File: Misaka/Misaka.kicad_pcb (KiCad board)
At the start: 2 copper layers, 100 x 100 mm, 106 parts, among them J1 Conn_Coaxial_Power, J2 Conn_01x04_Male, J3 Conn_01x04_Male, J4 Conn_01x04_Male, J5 USB_B_Micro, J6 Conn_01x04_Female, J7 Conn_01x04_Female_UART, J8 Conn_02x04_Odd_Even, J9 Conn_01x07, SW1 SW_DIP_x03, U1 DRV8825PWPR, U2 ATmega2560-16AU, U3 DRV8825PWPR, U4 DRV8825PWPR, U5 CH340C, U6 AMS1117-5.0, U7 AMS1117-3.3, U8 24LC02, Y1 CSTLS16M0X51-B0

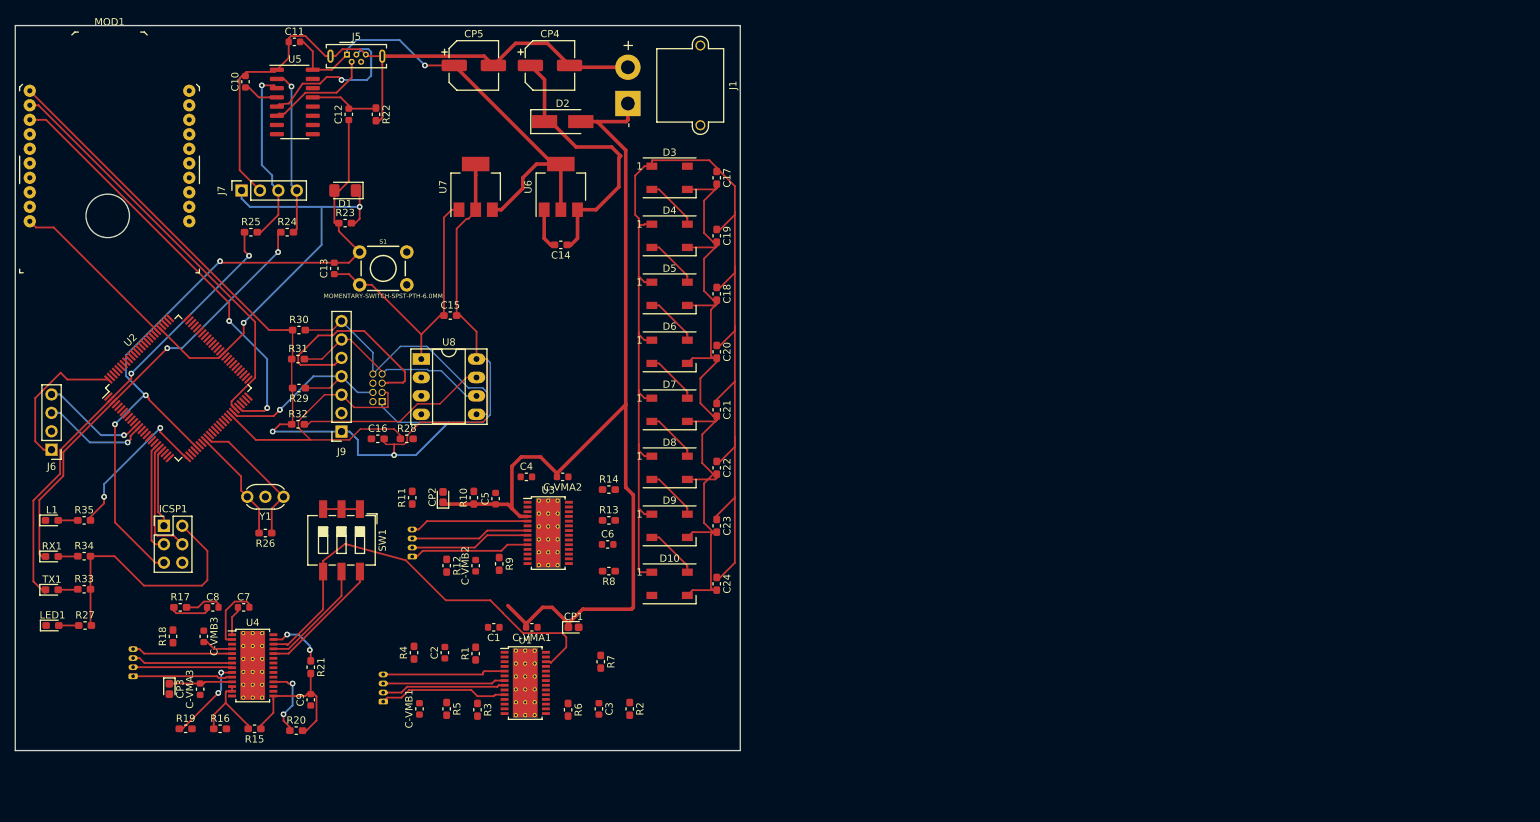
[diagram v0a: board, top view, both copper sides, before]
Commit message: change footprint to handsolding
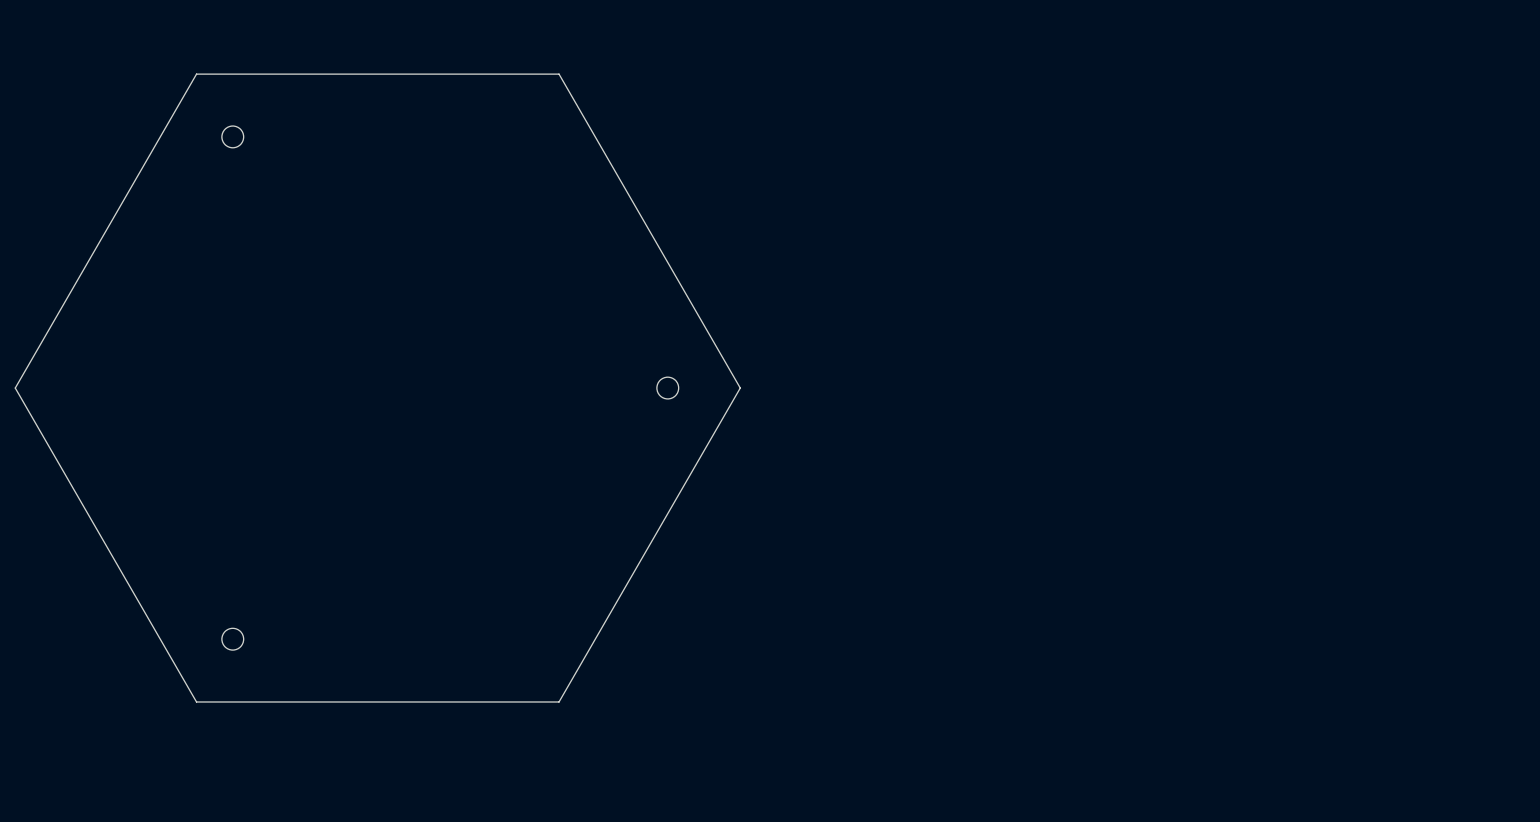
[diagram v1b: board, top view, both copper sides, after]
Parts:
- removed C-VMA1, C-VMA2, C-VMA3, C-VMB1, C-VMB2, C-VMB3, C2, C5, C8: 0.1uF, Capacitor_SMD:C_0603_1608Metric
- removed C1, C4, C7: 0.01uF, Capacitor_SMD:C_0603_1608Metric
- removed C10, C11, C12: 100nF, Capacitor_SMD:C_0603_1608Metric
- removed C13: 22pF, Capacitor_SMD:C_0603_1608Metric
- removed C14, C17, C18, C19, C20, C21, C22, C23, C24: 100nF, Capacitor_SMD:C_0603_1608Metric_Pad1.05x0.95mm_HandSolder
- removed C15, C16: 1uF, Capacitor_SMD:C_0603_1608Metric_Pad1.05x0.95mm_HandSolder
- removed C3, C6, C9: 0.47uF, Capacitor_SMD:C_0603_1608Metric
- removed CP1, CP2, CP3: 100uF, Capacitor_Tantalum_SMD:CP_EIA-1608-08_AVX-J
- removed CP4, CP5: 47uF, Capacitor_SMD:CP_Elec_6.3x5.8
- removed D1: CD1206, Diode_SMD:D_1206_3216Metric_Pad1.42x1.75mm_HandSolder
- removed D10, D3, D4, D5, D6, D7, D8, D9: WS2812B, LED_SMD:LED_WS2812B_PLCC4_5.0x5.0mm_P3.2mm
- removed D2: M7, Diode_SMD:D_SMA_Handsoldering
- removed ICSP1: Conn_02x03_Odd_Even, Connector_PinHeader_2.54mm:PinHeader_2x03_P2.54mm_Vertical
- removed J1: Conn_Coaxial_Power, Connector_AMASS:AMASS_XT30PW-M_1x02_P2.50mm_Horizontal
- removed J2, J3, J4: Conn_01x04_Male, Connector_Molex:Molex_PicoBlade_53047-0410_1x04_P1.25mm_Vertical
- removed J5: USB_B_Micro, Connector_USB:USB_Micro-B_Wuerth_614105150721_Vertical
- removed J6: Conn_01x04_Female, Connector_PinHeader_2.54mm:PinHeader_1x04_P2.54mm_Vertical
- removed J7: Conn_01x04_Female_UART, Connector_PinSocket_2.54mm:PinSocket_1x04_P2.54mm_Vertical
- removed J8: Conn_02x04_Odd_Even, Connector_PinSocket_1.27mm:PinSocket_2x04_P1.27mm_Vertical
- removed J9: Conn_01x07, Connector_PinSocket_2.54mm:PinSocket_1x07_P2.54mm_Vertical
- removed L1, RX1, TX1: LED, LED_SMD:LED_0603_1608Metric_Pad1.05x0.95mm_HandSolder
- removed LED1: ON, LED_SMD:LED_0603_1608Metric_Pad1.05x0.95mm_HandSolder
- removed MOD1: XB24CZ7PIT-004, digikey-footprints:XBEE_PRO-20_THT
- removed R1, R10, R17, R26: 1M, Resistor_SMD:R_0603_1608Metric_Pad1.05x0.95mm_HandSolder
- removed R11, R12, R18, R19, R4, R5: 200m, Resistor_SMD:R_0603_1608Metric_Pad1.05x0.95mm_HandSolder
- removed R13, R14, R20, R21, R6, R7: 10K, Resistor_SMD:R_0603_1608Metric_Pad1.05x0.95mm_HandSolder
- removed R15, R2, R8: 50K, Resistor_SMD:R_0603_1608Metric_Pad1.05x0.95mm_HandSolder
- removed R16, R3, R9: 30K, Resistor_SMD:R_0603_1608Metric_Pad1.05x0.95mm_HandSolder
- removed R22, R24, R25, R27, R28, R33, R34, R35: 1k, Resistor_SMD:R_0603_1608Metric_Pad1.05x0.95mm_HandSolder
- removed R23: 10k, Resistor_SMD:R_0603_1608Metric_Pad1.05x0.95mm_HandSolder
- removed R29, R30, R31, R32: 4.7k, Resistor_SMD:R_0603_1608Metric_Pad1.05x0.95mm_HandSolder
- removed S1: MOMENTARY-SWITCH-SPST-PTH-6.0MM, Switches:TACTILE_SWITCH_PTH_6.0MM
- removed SW1: SW_DIP_x03, Button_Switch_SMD:SW_DIP_SPSTx03_Slide_6.7x9.18mm_W8.61mm_P2.54mm_LowProfile
- removed U1, U3, U4: DRV8825PWPR, Package_SO:HTSSOP-28-1EP_4.4x9.7mm_P0.65mm_EP3.4x9.5mm_ThermalVias
- removed U2: ATmega2560-16AU, Package_QFP:TQFP-100_14x14mm_P0.5mm
- removed U5: CH340C, Package_SO:SOIC-16_3.9x9.9mm_P1.27mm
- removed U6: AMS1117-5.0, Package_TO_SOT_SMD:SOT-223-3_TabPin2
- removed U7: AMS1117-3.3, Package_TO_SOT_SMD:SOT-223-3_TabPin2
- removed U8: 24LC02, Package_DIP:DIP-8_W7.62mm_Socket_LongPads
- removed Y1: CSTLS16M0X51-B0, Crystal:Resonator_muRata_CSTLSxxxX-3Pin_W5.5mm_H3.0mm
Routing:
- net +5V: track 357.3 -> 0.00 mm, vias 3 -> 0
- net GND: track 258.7 -> 0.00 mm
- net +3V3: track 179.3 -> 0.00 mm, vias 2 -> 0
- net +12V: track 158.8 -> 0.00 mm
- net /RESET: track 104.9 -> 0.00 mm, vias 3 -> 0
- net /RX0: track 63.5 -> 0.00 mm, vias 2 -> 0
- net /TX0: track 60.4 -> 0.00 mm, vias 2 -> 0
- net /MS3: track 59.8 -> 0.00 mm
- net /TX1: track 59.0 -> 0.00 mm, vias 2 -> 0
- net /RX1: track 57.1 -> 0.00 mm
- net /SCL: track 47.0 -> 0.00 mm
- net /CameraModule/E2PROM-SDA: track 39.1 -> 0.00 mm
- net Net-(C14-Pad1): track 38.1 -> 0.00 mm
- net /CameraModule/EFUSE: track 30.5 -> 0.00 mm
- net /CameraModule/E2PROM-SCK: track 28.8 -> 0.00 mm
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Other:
- board size 100 x 100 mm -> 100 x 86.6 mm

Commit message: route v2.0
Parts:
- added C-VMA1: 0.1uF, Capacitor_SMD:C_0603_1608Metric_Pad1.05x0.95mm_HandSolder, B.Cu at (164.3, 119.7)
- added C-VMA2: 0.1uF, Capacitor_SMD:C_0603_1608Metric_Pad1.05x0.95mm_HandSolder, B.Cu at (205.9, 121.4)
- added C-VMA3: 0.1uF, Capacitor_SMD:C_0603_1608Metric_Pad1.05x0.95mm_HandSolder, B.Cu at (229.9, 124.9)
- added C-VMB1: 0.1uF, Capacitor_SMD:C_0603_1608Metric_Pad1.05x0.95mm_HandSolder, B.Cu at (168.7, 119.7)
- added C-VMB2: 0.1uF, Capacitor_SMD:C_0603_1608Metric_Pad1.05x0.95mm_HandSolder, B.Cu at (205.7, 126.5)
- added C-VMB3: 0.1uF, Capacitor_SMD:C_0603_1608Metric_Pad1.05x0.95mm_HandSolder, B.Cu at (230.2, 122.4)
- added C1: 0.01uF, Capacitor_SMD:C_0603_1608Metric_Pad1.05x0.95mm_HandSolder, B.Cu at (181.5, 123.5)
- added C10: 100nF, Capacitor_SMD:C_0603_1608Metric_Pad1.05x0.95mm_HandSolder, F.Cu at (97.9, 101.9)
- added C11: 100nF, Capacitor_SMD:C_0603_1608Metric_Pad1.05x0.95mm_HandSolder, F.Cu at (105.6, 97.0)
- added C12: 100nF, Capacitor_SMD:C_0603_1608Metric_Pad1.05x0.95mm_HandSolder, F.Cu at (106.6, 99.5)
- added C13: 22pF, Capacitor_SMD:C_0603_1608Metric_Pad1.05x0.95mm_HandSolder, F.Cu at (102.2, 101.9)
- added C14: 100nF, Capacitor_SMD:C_0603_1608Metric_Pad1.05x0.95mm_HandSolder, F.Cu at (191.9, 86.9)
- added C15: 1uF, Capacitor_SMD:C_0603_1608Metric_Pad1.05x0.95mm_HandSolder, F.Cu at (84.7, 80.1)
- added C16: 1uF, Capacitor_SMD:C_0603_1608Metric_Pad1.05x0.95mm_HandSolder, F.Cu at (71.2, 95.4)
- added C17: 100nF, Capacitor_SMD:C_0603_1608Metric_Pad1.05x0.95mm_HandSolder, F.Cu at (202.3, 52.3)
- added C18: 100nF, Capacitor_SMD:C_0603_1608Metric_Pad1.05x0.95mm_HandSolder, F.Cu at (215.3, 52.3)
- added C19: 100nF, Capacitor_SMD:C_0603_1608Metric_Pad1.05x0.95mm_HandSolder, F.Cu at (211.0, 52.3)
- added C2: 0.1uF, Capacitor_SMD:C_0603_1608Metric_Pad1.05x0.95mm_HandSolder, B.Cu at (181.5, 131.0)
- added C20: 100nF, Capacitor_SMD:C_0603_1608Metric_Pad1.05x0.95mm_HandSolder, F.Cu at (215.3, 49.8)
- added C21: 100nF, Capacitor_SMD:C_0603_1608Metric_Pad1.05x0.95mm_HandSolder, F.Cu at (206.7, 49.8)
- added C22: 100nF, Capacitor_SMD:C_0603_1608Metric_Pad1.05x0.95mm_HandSolder, F.Cu at (202.3, 49.8)
- added C23: 100nF, Capacitor_SMD:C_0603_1608Metric_Pad1.05x0.95mm_HandSolder, F.Cu at (206.7, 52.3)
- added C24: 100nF, Capacitor_SMD:C_0603_1608Metric_Pad1.05x0.95mm_HandSolder, F.Cu at (211.0, 49.8)
- added C3: 0.47uF, Capacitor_SMD:C_0603_1608Metric_Pad1.05x0.95mm_HandSolder, B.Cu at (181.8, 121.0)
- added C4: 0.01uF, Capacitor_SMD:C_0603_1608Metric_Pad1.05x0.95mm_HandSolder, B.Cu at (205.7, 123.9)
- added C5: 0.1uF, Capacitor_SMD:C_0603_1608Metric_Pad1.05x0.95mm_HandSolder, B.Cu at (201.6, 121.2)
- added C6: 0.47uF, Capacitor_SMD:C_0603_1608Metric_Pad1.05x0.95mm_HandSolder, B.Cu at (197.2, 121.0)
- added C7: 0.01uF, Capacitor_SMD:C_0603_1608Metric_Pad1.05x0.95mm_HandSolder, B.Cu at (221.1, 124.5)
- added C8: 0.1uF, Capacitor_SMD:C_0603_1608Metric_Pad1.05x0.95mm_HandSolder, B.Cu at (212.8, 121.1)
- added C9: 0.47uF, Capacitor_SMD:C_0603_1608Metric_Pad1.05x0.95mm_HandSolder, B.Cu at (217.1, 121.1)
- added CP1: 100uF, Capacitor_Tantalum_SMD:CP_EIA-1608-08_AVX-J_Pad1.25x1.05mm_HandSolder, B.Cu at (172.8, 125.7)
- added CP2: 100uF, Capacitor_Tantalum_SMD:CP_EIA-1608-08_AVX-J_Pad1.25x1.05mm_HandSolder, B.Cu at (196.9, 126.1)
- added CP3: 100uF, Capacitor_Tantalum_SMD:CP_EIA-1608-08_AVX-J_Pad1.25x1.05mm_HandSolder, B.Cu at (221.2, 127.1)
- added CP4: 47uF, Capacitor_SMD:CP_Elec_6.3x5.8, F.Cu at (180.1, 85.1)
- added CP5: 47uF, Capacitor_SMD:CP_Elec_6.3x5.8, F.Cu at (180.1, 76.9)
- added D1: CD1206, Diode_SMD:D_1206_3216Metric_Pad1.42x1.75mm_HandSolder, F.Cu at (84.0, 102.2)
- added D10: WS2812B, LED_SMD:LED_WS2812B_PLCC4_5.0x5.0mm_P3.2mm, F.Cu at (204.3, 45.2)
- added D2: M7, Diode_SMD:D_SMA_Handsoldering, F.Cu at (190.3, 75.1)
- added D3: WS2812B, LED_SMD:LED_WS2812B_PLCC4_5.0x5.0mm_P3.2mm, F.Cu at (229.6, 45.2)
- added D4: WS2812B, LED_SMD:LED_WS2812B_PLCC4_5.0x5.0mm_P3.2mm, F.Cu at (229.6, 38.6)
- added D5: WS2812B, LED_SMD:LED_WS2812B_PLCC4_5.0x5.0mm_P3.2mm, F.Cu at (221.2, 45.2)
- added D6: WS2812B, LED_SMD:LED_WS2812B_PLCC4_5.0x5.0mm_P3.2mm, F.Cu at (221.2, 38.6)
- added D7: WS2812B, LED_SMD:LED_WS2812B_PLCC4_5.0x5.0mm_P3.2mm, F.Cu at (204.3, 38.6)
- added D8: WS2812B, LED_SMD:LED_WS2812B_PLCC4_5.0x5.0mm_P3.2mm, F.Cu at (212.8, 45.2)
- added D9: WS2812B, LED_SMD:LED_WS2812B_PLCC4_5.0x5.0mm_P3.2mm, F.Cu at (212.8, 38.6)
- added ICSP1: Conn_02x03_Odd_Even, Connector_PinHeader_2.54mm:PinHeader_2x03_P2.54mm_Vertical, F.Cu at (182.4, 54.5)
- added J1: Conn_Coaxial_Power, Connector_AMASS:AMASS_XT30PW-M_1x02_P2.50mm_Horizontal, F.Cu at (54.8, 104.2)
- added J2: Conn_01x04_Male, Connector_Molex:Molex_PicoBlade_53047-0410_1x04_P1.25mm_Vertical, B.Cu at (173.1, 129.2)
- added J3: Conn_01x04_Male, Connector_Molex:Molex_PicoBlade_53047-0410_1x04_P1.25mm_Vertical, B.Cu at (197.2, 129.7)
- added J4: Conn_01x04_Male, Connector_Molex:Molex_PicoBlade_53047-0410_1x04_P1.25mm_Vertical, B.Cu at (221.5, 130.6)
- added J5: USB_B_Micro, Connector_USB:USB_Micro-B_Wuerth_614105150721_Vertical, F.Cu at (97.8, 90.5)
- added J6: Conn_01x04_Female, Connector_PinHeader_2.54mm:PinHeader_1x04_P2.54mm_Vertical, F.Cu at (212.9, 76.6)
- added J7: Conn_01x04_Female_UART, Connector_PinSocket_2.54mm:PinSocket_1x04_P2.54mm_Vertical, F.Cu at (83.3, 90.6)
- added J8: Conn_02x04_Odd_Even, Connector_PinSocket_1.27mm:PinSocket_2x04_P1.27mm_Vertical, B.Cu at (75.7, 76.9)
- added J9: Conn_01x07, Connector_PinSocket_2.54mm:PinSocket_1x07_P2.54mm_Vertical, F.Cu at (67.5, 71.5)
- added L1: LED, LED_SMD:LED_0603_1608Metric_Pad1.05x0.95mm_HandSolder, F.Cu at (61.3, 55.6)
- added LED1: ON, LED_SMD:LED_0603_1608Metric_Pad1.05x0.95mm_HandSolder, F.Cu at (187.5, 87.0)
- added MOD1: XB24CZ7PIT-004, digikey-footprints:XBEE_PRO-20_THT, F.Cu at (87.5, 49.5)
- added R1: 1M, Resistor_SMD:R_0603_1608Metric_Pad1.05x0.95mm_HandSolder, B.Cu at (172.7, 123.1)
- added R10: 1M, Resistor_SMD:R_0603_1608Metric_Pad1.05x0.95mm_HandSolder, B.Cu at (192.9, 120.1)
- added R11: 200m, Resistor_SMD:R_0603_1608Metric_Pad1.05x0.95mm_HandSolder, B.Cu at (196.9, 123.5)
- added R12: 200m, Resistor_SMD:R_0603_1608Metric_Pad1.05x0.95mm_HandSolder, B.Cu at (201.3, 126.2)
- added R13: 10K, Resistor_SMD:R_0603_1608Metric_Pad1.05x0.95mm_HandSolder, B.Cu at (205.7, 129.0)
- added R14: 10K, Resistor_SMD:R_0603_1608Metric_Pad1.05x0.95mm_HandSolder, B.Cu at (201.3, 123.7)
- added R15: 50K, Resistor_SMD:R_0603_1608Metric_Pad1.05x0.95mm_HandSolder, B.Cu at (225.6, 127.2)
- added R16: 30K, Resistor_SMD:R_0603_1608Metric_Pad1.05x0.95mm_HandSolder, B.Cu at (229.9, 129.9)
- added R17: 1M, Resistor_SMD:R_0603_1608Metric_Pad1.05x0.95mm_HandSolder, B.Cu at (225.6, 124.7)
- added R18: 200m, Resistor_SMD:R_0603_1608Metric_Pad1.05x0.95mm_HandSolder, B.Cu at (221.5, 122.0)
- added R19: 200m, Resistor_SMD:R_0603_1608Metric_Pad1.05x0.95mm_HandSolder, B.Cu at (229.9, 127.4)
- added R2: 50K, Resistor_SMD:R_0603_1608Metric_Pad1.05x0.95mm_HandSolder, B.Cu at (177.2, 125.8)
- added R20: 10K, Resistor_SMD:R_0603_1608Metric_Pad1.05x0.95mm_HandSolder, B.Cu at (225.8, 122.1)
- added R21: 10K, Resistor_SMD:R_0603_1608Metric_Pad1.05x0.95mm_HandSolder, B.Cu at (229.9, 132.4)
- added R22: 1k, Resistor_SMD:R_0603_1608Metric_Pad1.05x0.95mm_HandSolder, F.Cu at (105.6, 94.5)
- added R23: 10k, Resistor_SMD:R_0603_1608Metric_Pad1.05x0.95mm_HandSolder, F.Cu at (93.5, 101.9)
- added R24: 1k, Resistor_SMD:R_0603_1608Metric_Pad1.05x0.95mm_HandSolder, F.Cu at (89.2, 101.0)
- added R25: 1k, Resistor_SMD:R_0603_1608Metric_Pad1.05x0.95mm_HandSolder, F.Cu at (106.3, 89.5)
- added R26: 1M, Resistor_SMD:R_0603_1608Metric_Pad1.05x0.95mm_HandSolder, F.Cu at (47.2, 93.7)
- added R27: 1k, Resistor_SMD:R_0603_1608Metric_Pad1.05x0.95mm_HandSolder, F.Cu at (197.3, 82.4)
- added R28: 1k, Resistor_SMD:R_0603_1608Metric_Pad1.05x0.95mm_HandSolder, F.Cu at (71.2, 97.9)
- added R29: 4.7k, Resistor_SMD:R_0603_1608Metric_Pad1.05x0.95mm_HandSolder, F.Cu at (84.5, 76.5)
- added R3: 30K, Resistor_SMD:R_0603_1608Metric_Pad1.05x0.95mm_HandSolder, B.Cu at (181.5, 128.5)
- added R30: 4.7k, Resistor_SMD:R_0603_1608Metric_Pad1.05x0.95mm_HandSolder, F.Cu at (75.6, 95.4)
- added R31: 4.7k, Resistor_SMD:R_0603_1608Metric_Pad1.05x0.95mm_HandSolder, F.Cu at (71.2, 100.4)
- added R32: 4.7k, Resistor_SMD:R_0603_1608Metric_Pad1.05x0.95mm_HandSolder, F.Cu at (84.2, 72.2)
- added R33: 1k, Resistor_SMD:R_0603_1608Metric_Pad1.05x0.95mm_HandSolder, F.Cu at (65.6, 58.2)
- added R34: 1k, Resistor_SMD:R_0603_1608Metric_Pad1.05x0.95mm_HandSolder, F.Cu at (65.6, 55.6)
- added R35: 1k, Resistor_SMD:R_0603_1608Metric_Pad1.05x0.95mm_HandSolder, F.Cu at (61.2, 58.2)
- added R4: 200m, Resistor_SMD:R_0603_1608Metric_Pad1.05x0.95mm_HandSolder, B.Cu at (177.2, 123.3)
- added R5: 200m, Resistor_SMD:R_0603_1608Metric_Pad1.05x0.95mm_HandSolder, B.Cu at (173.1, 120.6)
- added R6: 10K, Resistor_SMD:R_0603_1608Metric_Pad1.05x0.95mm_HandSolder, B.Cu at (181.5, 126.0)
- added R7: 10K, Resistor_SMD:R_0603_1608Metric_Pad1.05x0.95mm_HandSolder, B.Cu at (177.4, 120.8)
- added R8: 50K, Resistor_SMD:R_0603_1608Metric_Pad1.05x0.95mm_HandSolder, B.Cu at (188.5, 120.1)
- added R9: 30K, Resistor_SMD:R_0603_1608Metric_Pad1.05x0.95mm_HandSolder, B.Cu at (205.7, 131.5)
- added RX1: LED, LED_SMD:LED_0603_1608Metric_Pad1.05x0.95mm_HandSolder, F.Cu at (56.9, 55.6)
- added S1: MOMENTARY-SWITCH-SPST-PTH-6.0MM, Switches:TACTILE_SWITCH_PTH_6.0MM, F.Cu at (98.7, 96.9)
- added SW1: SW_DIP_x03, Button_Switch_SMD:SW_DIP_SPSTx03_Slide_6.7x9.18mm_W8.61mm_P2.54mm_LowProfile, F.Cu at (203.0, 63.5)
- added TX1: LED, LED_SMD:LED_0603_1608Metric_Pad1.05x0.95mm_HandSolder, F.Cu at (56.9, 58.2)
- added U1: DRV8825PWPR, Package_SO:HTSSOP-28-1EP_4.4x9.7mm_P0.65mm_EP3.4x9.5mm_ThermalVias, B.Cu at (166.3, 126.6)
- added U2: ATmega2560-16AU, Package_QFP:TQFP-100_14x14mm_P0.5mm, F.Cu at (49.9, 76.8)
- added U3: DRV8825PWPR, Package_SO:HTSSOP-28-1EP_4.4x9.7mm_P0.65mm_EP3.4x9.5mm_ThermalVias, B.Cu at (190.5, 127.0)
- added U4: DRV8825PWPR, Package_SO:HTSSOP-28-1EP_4.4x9.7mm_P0.65mm_EP3.4x9.5mm_ThermalVias, B.Cu at (214.8, 128.0)
- added U5: CH340C, Package_SO:SOIC-16_3.9x9.9mm_P1.27mm, F.Cu at (89.8, 94.0)
- added U6: AMS1117-5.0, Package_TO_SOT_SMD:SOT-223-3_TabPin2, F.Cu at (200.3, 77.0)
- added U7: AMS1117-3.3, Package_TO_SOT_SMD:SOT-223-3_TabPin2, F.Cu at (190.2, 81.5)
- added U8: 24LC02, Package_DIP:DIP-8_W7.62mm_Socket_LongPads, F.Cu at (71.2, 84.4)
- added Y1: CSTLS16M0X51-B0, Crystal:Resonator_muRata_CSTLSxxxX-3Pin_W5.5mm_H3.0mm, F.Cu at (50.1, 89.4)
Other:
- net class Default: trace_width 0.25 -> 0.254
- net class Power added: clearance 0.254, trace_width 0.5, via_dia 1.2, via_drill 0.7
- rule trace_min: 0.2 -> 0.12

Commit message: route v2.1
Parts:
- moved ICSP1 152.1 mm to (32.1, 77.6), turned to 180 degrees
- moved C14 67.5 mm to (137.2, 47.3)
- moved CP5 67.5 mm to (125.4, 37.3)
- moved D2 67.5 mm to (135.7, 35.5)
- moved J6 67.5 mm to (158.3, 37.0)
- moved R27 67.5 mm to (142.7, 42.8)
- moved U6 67.5 mm to (145.6, 37.4)
- moved U7 67.5 mm to (135.6, 41.9)
- moved CP4 67.5 mm to (125.4, 45.5)
- moved LED1 67.5 mm to (132.9, 47.4)
- moved R35 13.4 mm to (49.0, 63.7)
- moved TX1 13.4 mm to (44.7, 63.8)
- moved L1 13.4 mm to (49.1, 61.2)
- moved R34 13.4 mm to (53.4, 61.1)
- moved RX1 13.4 mm to (44.7, 61.2)
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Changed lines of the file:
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@@
   )
   (module Package_TO_SOT_SMD:SOT-223-3_TabPin2 (layer F.Cu)
-    (at 190.22 81.53)
+    (at 135.57 41.93)
     (descr "module CMS SOT223 4 pins")
     (tags "CMS SOT")
@@
   )
   (module Package_TO_SOT_SMD:SOT-223-3_TabPin2 (layer F.Cu)
-    (at 200.27 76.98)
+    (at 145.62 37.38)
     (descr "module CMS SOT223 4 pins")
     (tags "CMS SOT")
@@
   )
   (module LED_SMD:LED_0603_1608Metric_Pad1.05x0.95mm_HandSolder (layer F.Cu)
-    (at 56.905 58.23)
+    (at 44.705 63.78)
     (descr "LED SMD 0603 (1608 Metric), square (rectangular) end terminal, IPC_7351 nominal, (Body size source: http://www.tortai-tech.com/upload/download/2011102023233369053.pdf), generated with kicad-footprint-generator")
     (tags "LED handsolder")
@@
   )
   (module LED_SMD:LED_0603_1608Metric_Pad1.05x0.95mm_HandSolder (layer F.Cu)
-    (at 56.905 55.64)
+    (at 44.705 61.19)
     (descr "LED SMD 0603 (1608 Metric), square (rectangular) end terminal, IPC_7351 nominal, (Body size source: http://www.tortai-tech.com/upload/download/2011102023233369053.pdf), generated with kicad-footprint-generator")
     (tags "LED handsolder")
@@
   )
   (module Resistor_SMD:R_0603_1608Metric_Pad1.05x0.95mm_HandSolder (layer F.Cu)
-    (at 61.25 58.19)
+    (at 49.05 63.74)
     (descr "Resistor SMD 0603 (1608 Metric), square (rectangular) end terminal, IPC_7351 nominal with elongated pad for handsoldering. (Body size source: http://www.tortai-tech.com/upload/download/2011102023233369053.pdf), generated with kicad-footprint-generator")
     (tags "resistor handsolder")
@@
   )
   (module Resistor_SMD:R_0603_1608Metric_Pad1.05x0.95mm_HandSolder (layer F.Cu)
-    (at 65.64 55.6)
+    (at 53.44 61.15)
     (descr "Resistor SMD 0603 (1608 Metric), square (rectangular) end terminal, IPC_7351 nominal with elongated pad for handsoldering. (Body size source: http://www.tortai-tech.com/upload/download/2011102023233369053.pdf), generated with kicad-footprint-generator")
     (tags "resistor handsolder")
@@
   )
   (module Resistor_SMD:R_0603_1608Metric_Pad1.05x0.95mm_HandSolder (layer F.Cu)
-    (at 65.6 58.19)
+    (at 53.4 63.74)
     (descr "Resistor SMD 0603 (1608 Metric), square (rectangular) end terminal, IPC_7351 nominal with elongated pad for handsoldering. (Body size source: http://www.tortai-tech.com/upload/download/2011102023233369053.pdf), generated with kicad-footprint-generator")
     (tags "resistor handsolder")
@@
   )
   (module Resistor_SMD:R_0603_1608Metric_Pad1.05x0.95mm_HandSolder (layer F.Cu)
-    (at 197.32 82.36)
+    (at 142.67 42.76)
     (descr "Resistor SMD 0603 (1608 Metric), square (rectangular) end terminal, IPC_7351 nominal with elongated pad for handsoldering. (Body size source: http://www.tortai-tech.com/upload/download/2011102023233369053.pdf), generated with kicad-footprint-generator")
     (tags "resistor handsolder")
@@
   )
   (module LED_SMD:LED_0603_1608Metric_Pad1.05x0.95mm_HandSolder (layer F.Cu)
-    (at 187.515 86.95)
+    (at 132.865 47.35)
     (descr "LED SMD 0603 (1608 Metric), square (rectangular) end terminal, IPC_7351 nominal, (Body size source: http://www.tortai-tech.com/upload/download/2011102023233369053.pdf), generated with kicad-footprint-generator")
     (tags "LED handsolder")
@@
   )
   (module LED_SMD:LED_0603_1608Metric_Pad1.05x0.95mm_HandSolder (layer F.Cu)
-    (at 61.295 55.64)
+    (at 49.095 61.19)
     (descr "LED SMD 0603 (1608 Metric), square (rectangular) end terminal, IPC_7351 nominal, (Body size source: http://www.tortai-tech.com/upload/download/2011102023233369053.pdf), generated with kicad-footprint-generator")
     (tags "LED handsolder")
@@
   )
   (module Connector_PinHeader_2.54mm:PinHeader_1x04_P2.54mm_Vertical (layer F.Cu)
-    (at 212.91 76.56)
+    (at 158.26 36.96)
     (descr "Through hole straight pin header, 1x04, 2.54mm pitch, single row")
     (tags "Through hole pin header THT 1x04 2.54mm single row")
@@
   )
   (module Connector_PinHeader_2.54mm:PinHeader_2x03_P2.54mm_Vertical (layer F.Cu)
-    (at 182.4 54.51)
+    (at 32.1 77.6 180)
     (descr "Through hole straight pin header, 2x03, 2.54mm pitch, double rows")
     (tags "Through hole pin header THT 2x03 2.54mm double row")
@@
     (fp_line (start 3.81 -1.27) (end 3.81 6.35) (layer F.Fab) (width 0.1))
     (fp_line (start 0 -1.27) (end 3.81 -1.27) (layer F.Fab) (width 0.1))
-    (pad 6 thru_hole oval (at 2.54 5.08) (size 1.7 1.7) (drill 1) (layers *.Cu *.Mask)
+    (pad 6 thru_hole oval (at 2.54 5.08 180) (size 1.7 1.7) (drill 1) (layers *.Cu *.Mask)
       (net 6 GND))
-    (pad 5 thru_hole oval (at 0 5.08) (size 1.7 1.7) (drill 1) (layers *.Cu *.Mask)
+    (pad 5 thru_hole oval (at 0 5.08 180) (size 1.7 1.7) (drill 1) (layers *.Cu *.Mask)
       (net 18 /RESET))
-    (pad 4 thru_hole oval (at 2.54 2.54) (size 1.7 1.7) (drill 1) (layers *.Cu *.Mask)
+    (pad 4 thru_hole oval (at 2.54 2.54 180) (size 1.7 1.7) (drill 1) (layers *.Cu *.Mask)
       (net 30 /MOSI))
-    (pad 3 thru_hole oval (at 0 2.54) (size 1.7 1.7) (drill 1) (layers *.Cu *.Mask)
+    (pad 3 thru_hole oval (at 0 2.54 180) (size 1.7 1.7) (drill 1) (layers *.Cu *.Mask)
       (net 31 /SCK))
-    (pad 2 thru_hole oval (at 2.54 0) (size 1.7 1.7) (drill 1) (layers *.Cu *.Mask)
+    (pad 2 thru_hole oval (at 2.54 0 180) (size 1.7 1.7) (drill 1) (layers *.Cu *.Mask)
       (net 16 +5V))
-    (pad 1 thru_hole rect (at 0 0) (size 1.7 1.7) (drill 1) (layers *.Cu *.Mask)
+    (pad 1 thru_hole rect (at 0 0 180) (size 1.7 1.7) (drill 1) (layers *.Cu *.Mask)
       (net 32 /MISO))
     (model ${KISYS3DMOD}/Connector_PinHeader_2.54mm.3dshapes/PinHeader_2x03_P2.54mm_Vertical.wrl
@@
   )
   (module Diode_SMD:D_SMA_Handsoldering (layer F.Cu)
-    (at 190.32 75.13)
+    (at 135.67 35.53)
     (descr "Diode SMA (DO-214AC) Handsoldering")
     (tags "Diode SMA (DO-214AC) Handsoldering")
@@
   )
   (module Capacitor_SMD:CP_Elec_6.3x5.8 (layer F.Cu)
-    (at 180.07 76.93)
+    (at 125.42 37.33)
     (descr "SMD capacitor, aluminum electrolytic, Nichicon, 6.3x5.8mm")
     (tags "capacitor electrolytic")
@@
   )
   (module Capacitor_SMD:CP_Elec_6.3x5.8 (layer F.Cu)
-    (at 180.07 85.08)
+    (at 125.42 45.48)
     (descr "SMD capacitor, aluminum electrolytic, Nichicon, 6.3x5.8mm")
     (tags "capacitor electrolytic")
@@
   )
   (module Capacitor_SMD:C_0603_1608Metric_Pad1.05x0.95mm_HandSolder (layer F.Cu)
-    (at 191.86 86.91)
+    (at 137.21 47.31)
     (descr "Capacitor SMD 0603 (1608 Metric), square (rectangular) end terminal, IPC_7351 nominal with elongated pad for handsoldering. (Body size source: http://www.tortai-tech.com/upload/download/2011102023233369053.pdf), generated with kicad-footprint-generator")
     (tags "capacitor handsolder")
